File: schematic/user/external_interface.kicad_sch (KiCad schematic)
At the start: 27 parts, among them J2 Radio_Jack, J3 User_Jack, J5 PTT Breakout, Q3 MBT3904DW1T1, Q4 MBT3904DW1T1, Q5 MBT3904DW1T1, SW3 PTT_Button, SW4 Mode_Button, SW5 Vol_Up_Button, SW6 Vol_Down_Button

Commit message: v0.6 board: add UART0 header to assist with ESP RF Test Tool.
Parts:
- J2, J3: footprint CUI_SJ-43514 -> ezDV_production:CUI_SJ-43514
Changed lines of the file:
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@@
     (property "Reference" "J3" (id 0) (at 91.44 21.7002 0))
     (property "Value" "User_Jack" (id 1) (at 91.44 24.2371 0))
-    (property "Footprint" "CUI_SJ-43514" (id 2) (at 91.44 33.02 0)
+    (property "Footprint" "ezDV_production:CUI_SJ-43514" (id 2) (at 91.44 33.02 0)
       (effects (font (size 1.27 1.27)) (justify bottom) hide)
     )
@@
     (property "Reference" "J2" (id 0) (at 30.48 22.9702 0))
     (property "Value" "Radio_Jack" (id 1) (at 30.48 25.5071 0))
-    (property "Footprint" "CUI_SJ-43514" (id 2) (at 30.48 34.29 0)
+    (property "Footprint" "ezDV_production:CUI_SJ-43514" (id 2) (at 30.48 34.29 0)
       (effects (font (size 1.27 1.27)) (justify bottom) hide)
     )

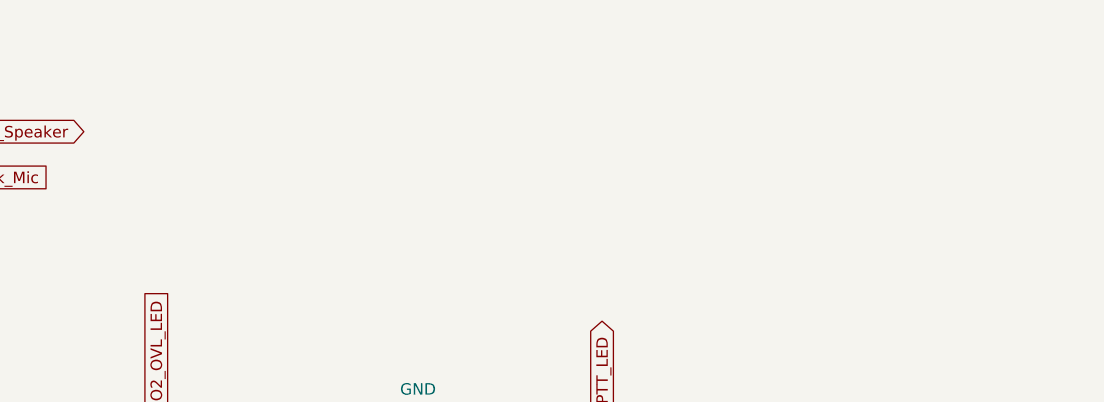
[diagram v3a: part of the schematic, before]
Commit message: v0.6 board: add breakouts for user and radio audio.
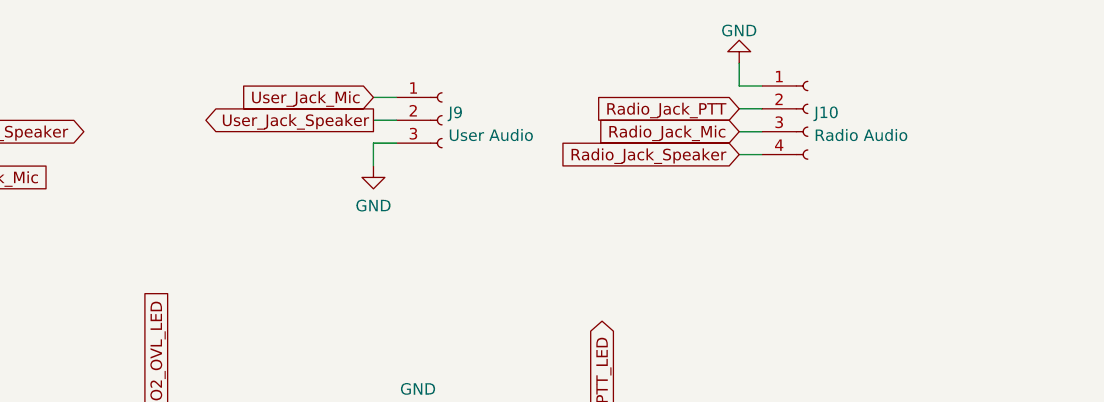
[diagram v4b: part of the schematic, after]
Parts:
- added J10: Radio Audio, Connector_PinHeader_2.54mm:PinHeader_1x04_P2.54mm_Vertical, symbol Connector:Conn_01x04_Female
- added J9: User Audio, Connector_PinSocket_2.54mm:PinSocket_1x03_P2.54mm_Vertical, symbol Connector:Conn_01x03_Female
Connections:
- net GND: now also J10.1 (Pin_1), J9.3 (Pin_3)
- net Radio_Jack_Mic: now also J10.3 (Pin_3)
- net Radio_Jack_PTT: now also J10.2 (Pin_2)
- net Radio_Jack_Speaker: now also J10.4 (Pin_4)
- net User_Jack_Mic: now also J9.1 (Pin_1)
- net User_Jack_Speaker: now also J9.2 (Pin_2)
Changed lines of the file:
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@@
+    (stroke (width 0) (type default) (color 0 0 0 0))
+  )
+  (wire (pts (xy 198.12 30.48) (xy 200.66 30.48))
     (stroke (width 0) (type default) (color 0 0 0 0))
   )
@@
     (stroke (width 0) (type default) (color 0 0 0 0))
   )
+  (wire (pts (xy 157.48 31.75) (xy 160.02 31.75))
+    (stroke (width 0) (type default) (color 0 0 0 0))
+  )
   (wire (pts (xy 22.86 129.54) (xy 26.67 129.54))
     (stroke (width 0) (type default) (color 0 0 0 0))
   )
+  (wire (pts (xy 198.12 27.94) (xy 198.12 25.4))
+    (stroke (width 0) (type default) (color 0 0 0 0))
+  )
+  (wire (pts (xy 157.48 29.21) (xy 160.02 29.21))
+    (stroke (width 0) (type default) (color 0 0 0 0))
+  )
   (wire (pts (xy 93.98 78.74) (xy 93.98 81.28))
     (stroke (width 0) (type default) (color 0 0 0 0))
@@
     (stroke (width 0) (type default) (color 0 0 0 0))
   )
+  (wire (pts (xy 198.12 35.56) (xy 200.66 35.56))
+    (stroke (width 0) (type default) (color 0 0 0 0))
+  )
   (wire (pts (xy 68.58 142.24) (xy 66.04 142.24))
     (stroke (width 0) (type default) (color 0 0 0 0))
@@
     (stroke (width 0) (type default) (color 0 0 0 0))
   )
+  (wire (pts (xy 198.12 33.02) (xy 200.66 33.02))
+    (stroke (width 0) (type default) (color 0 0 0 0))
+  )
   (wire (pts (xy 120.65 152.4) (xy 118.11 152.4))
     (stroke (width 0) (type default) (color 0 0 0 0))
@@
     (stroke (width 0) (type default) (color 0 0 0 0))
   )
+  (wire (pts (xy 157.48 34.29) (xy 160.02 34.29))
+    (stroke (width 0) (type default) (color 0 0 0 0))
+  )
   (wire (pts (xy 93.98 81.28) (xy 91.44 81.28))
     (stroke (width 0) (type default) (color 0 0 0 0))
@@
     (stroke (width 0) (type default) (color 0 0 0 0))
   )
+  (wire (pts (xy 200.66 27.94) (xy 198.12 27.94))
+    (stroke (width 0) (type default) (color 0 0 0 0))
+  )
   (wire (pts (xy 123.19 105.41) (xy 123.19 107.95))
     (stroke (width 0) (type default) (color 0 0 0 0))
@@
     (stroke (width 0) (type default) (color 0 0 0 0))
   )
+  (wire (pts (xy 157.48 36.83) (xy 157.48 34.29))
+    (stroke (width 0) (type default) (color 0 0 0 0))
+  )
   (wire (pts (xy 40.64 29.21) (xy 45.72 29.21))
     (stroke (width 0) (type default) (color 0 0 0 0))
@@
     (property "Intersheet References" "${INTERSHEET_REFS}" (id 0) (at -2.54 10.16 0)
       (effects (font (size 1.27 1.27)) hide)
+    )
+  )
+  (global_label "Radio_Jack_Mic" (shape input) (at 198.12 33.02 180) (fields_autoplaced)
+    (effects (font (size 1.27 1.27)) (justify right))
+    (property "Intersheet References" "${INTERSHEET_REFS}" (id 0) (at 181.0717 33.0994 0)
+      (effects (font (size 1.27 1.27)) (justify right) hide)
     )
   )
@@
     )
   )
+  (global_label "User_Jack_Mic" (shape input) (at 157.48 29.21 180) (fields_autoplaced)
+    (effects (font (size 1.27 1.27)) (justify right))
+    (property "Intersheet References" "${INTERSHEET_REFS}" (id 0) (at 141.5202 29.1306 0)
+      (effects (font (size 1.27 1.27)) (justify right) hide)
+    )
+  )
+  (global_label "Radio_Jack_Speaker" (shape input) (at 198.12 35.56 180) (fields_autoplaced)
+    (effects (font (size 1.27 1.27)) (justify right))
+    (property "Intersheet References" "${INTERSHEET_REFS}" (id 0) (at 240.03 69.85 0)
+      (effects (font (size 1.27 1.27)) hide)
+    )
+  )
+  (global_label "User_Jack_Speaker" (shape output) (at 157.48 31.75 180) (fields_autoplaced)
+    (effects (font (size 1.27 1.27)) (justify right))
+    (property "Intersheet References" "${INTERSHEET_REFS}" (id 0) (at 137.1659 31.6706 0)
+      (effects (font (size 1.27 1.27)) (justify right) hide)
+    )
+  )
   (global_label "GPIO4_PTT_IN" (shape output) (at 25.4 142.24 0) (fields_autoplaced)
     (effects (font (size 1.27 1.27)) (justify left))
@@
     )
   )
+  (global_label "Radio_Jack_PTT" (shape input) (at 198.12 30.48 180) (fields_autoplaced)
+    (effects (font (size 1.27 1.27)) (justify right))
+    (property "Intersheet References" "${INTERSHEET_REFS}" (id 0) (at 181.0112 30.4006 0)
+      (effects (font (size 1.27 1.27)) (justify right) hide)
+    )
+  )
   (global_label "GPIO1_SYNC_LED" (shape input) (at 93.98 68.58 90) (fields_autoplaced)
     (effects (font (size 1.27 1.27)) (justify left))
@@
     (pin "1")
     (pin "2")
+  )
+  (symbol (lib_id "Connector:Conn_01x04_Female") (at 205.74 30.48 0) (unit 1)
+    (in_bom yes) (on_board yes) (fields_autoplaced)
+    (property "Reference" "J10" (id 0) (at 206.4512 30.9153 0)
+      (effects (font (size 1.27 1.27)) (justify left))
+    )
+    (property "Value" "Radio Audio" (id 1) (at 206.4512 33.4522 0)
+      (effects (font (size 1.27 1.27)) (justify left))
+    )
+    (property "Footprint" "Connector_PinHeader_2.54mm:PinHeader_1x04_P2.54mm_Vertical" (id 2) (at 205.74 30.48 0)
+      (effects (font (size 1.27 1.27)) hide)
+    )
+    (property "Datasheet" "~" (id 3) (at 205.74 30.48 0)
+      (effects (font (size 1.27 1.27)) hide)
+    )
+    (pin "1")
+    (pin "2")
+    (pin "3")
+    (pin "4")
   )
   (symbol (lib_id "power:GND") (at 104.14 27.94 90) (unit 1)
@@
     (pin "1")
   )
+  (symbol (lib_id "power:GND") (at 157.48 36.83 0) (unit 1)
+    (in_bom yes) (on_board yes) (fields_autoplaced)
+    (property "Reference" "#PWR046" (id 0) (at 157.48 43.18 0)
+      (effects (font (size 1.27 1.27)) hide)
+    )
+    (property "Value" "GND" (id 1) (at 157.48 41.2734 0))
+    (property "Footprint" "" (id 2) (at 157.48 36.83 0)
+      (effects (font (size 1.27 1.27)) hide)
+    )
+    (property "Datasheet" "" (id 3) (at 157.48 36.83 0)
+      (effects (font (size 1.27 1.27)) hide)
+    )
+    (pin "1")
+  )
   (symbol (lib_id "power:GND") (at 123.19 72.39 180) (unit 1)
     (in_bom yes) (on_board yes)
@@
       (effects (font (size 1.27 1.27)) hide)
     )
+    (pin "1")
+  )
+  (symbol (lib_id "Connector:Conn_01x03_Female") (at 165.1 31.75 0) (unit 1)
+    (in_bom yes) (on_board yes) (fields_autoplaced)
+    (property "Reference" "J9" (id 0) (at 165.8112 30.9153 0)
+      (effects (font (size 1.27 1.27)) (justify left))
+    )
+    (property "Value" "User Audio" (id 1) (at 165.8112 33.4522 0)
+      (effects (font (size 1.27 1.27)) (justify left))
+    )
+    (property "Footprint" "Connector_PinSocket_2.54mm:PinSocket_1x03_P2.54mm_Vertical" (id 2) (at 165.1 31.75 0)
+      (effects (font (size 1.27 1.27)) hide)
+    )
+    (property "Datasheet" "~" (id 3) (at 165.1 31.75 0)
+      (effects (font (size 1.27 1.27)) hide)
+    )
+    (pin "1")
+    (pin "2")
+    (pin "3")
+  )
+  (symbol (lib_id "power:GND") (at 198.12 25.4 180) (unit 1)
+    (in_bom yes) (on_board yes) (fields_autoplaced)
+    (property "Reference" "#PWR047" (id 0) (at 198.12 19.05 0)
+      (effects (font (size 1.27 1.27)) hide)
+    )
+    (property "Value" "GND" (id 1) (at 198.12 21.8242 0))
+    (property "Footprint" "" (id 2) (at 198.12 25.4 0)
+      (effects (font (size 1.27 1.27)) hide)
+    )
+    (property "Datasheet" "" (id 3) (at 198.12 25.4 0)
+      (effects (font (size 1.27 1.27)) hide)
+    )

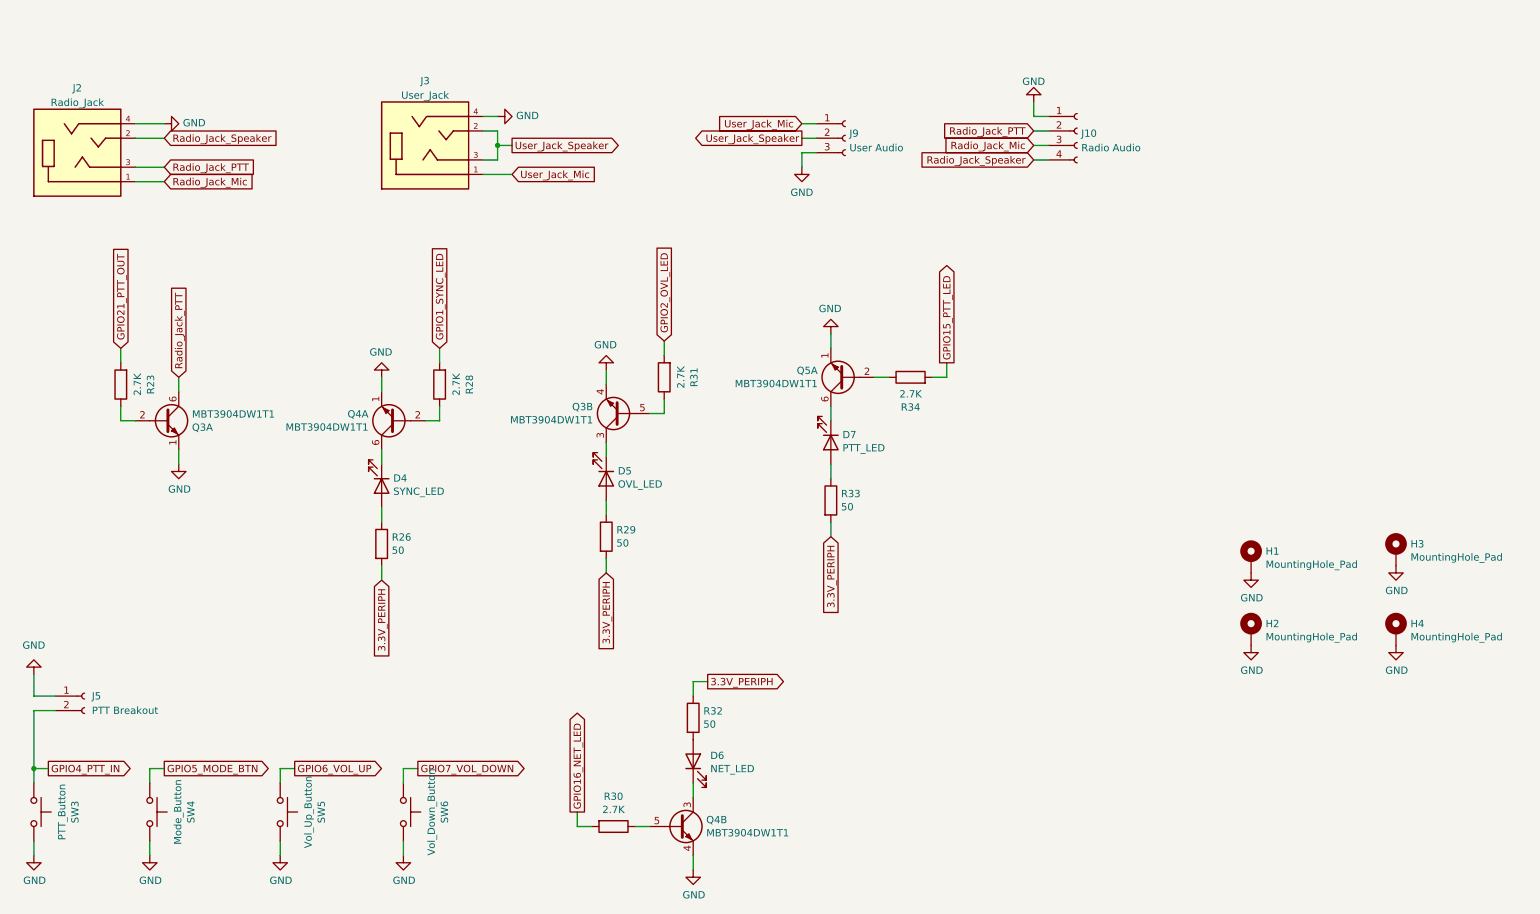
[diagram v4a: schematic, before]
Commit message: v0.6 board: add protection diodes on all connectors.
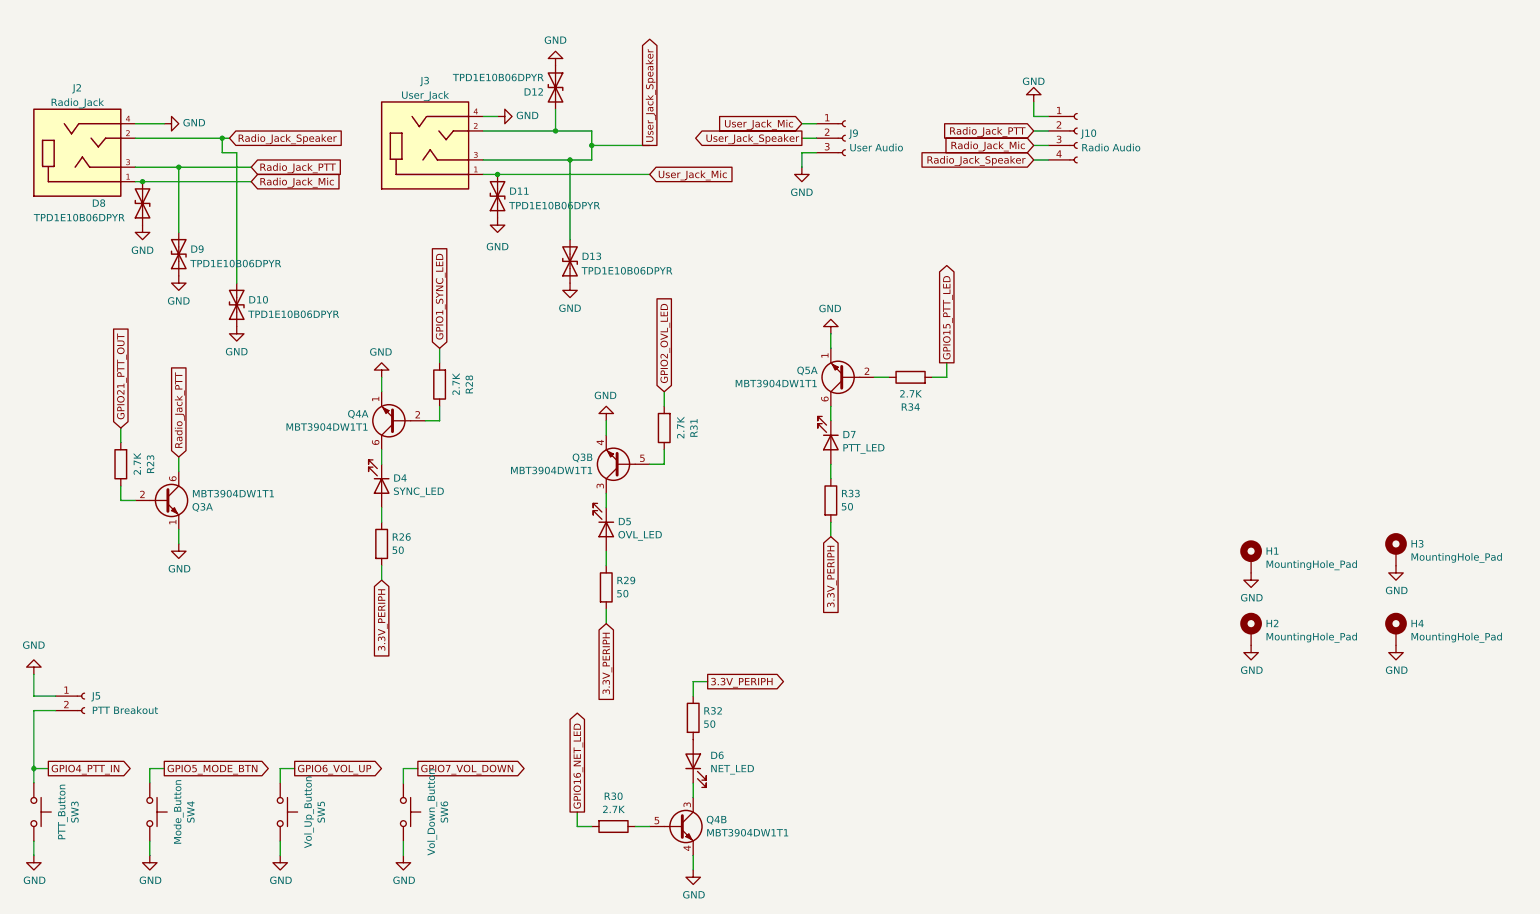
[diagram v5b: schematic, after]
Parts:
- added D10, D11, D12, D13, D8, D9: TPD1E10B06DPYR, ezDV_production:DIO_TPD1E05U06DPYR, symbol Device:D_TVS
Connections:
- net GND: now also D10.1 (A1), D11.1 (A1), D12.1 (A1), D13.1 (A1), D8.1 (A1), D9.1 (A1)
- net Radio_Jack_Mic: now also D8.2 (A2)
- net Radio_Jack_PTT: now also D9.2 (A2)
- net Radio_Jack_Speaker: now also D10.2 (A2)
- net User_Jack_Mic: now also D11.2 (A2)
- net User_Jack_Speaker: now also D12.2 (A2), D13.2 (A2)
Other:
- moved on the sheet: D5, Q3A, Q3B, R23, R29, R31
